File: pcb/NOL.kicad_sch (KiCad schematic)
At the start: 70 parts, among them J1 Conn_01x10_Socket, J10 Conn_01x02_Socket, J11 Conn_01x02_Socket, J12 Conn_01x02_Socket, J13 Conn_01x02_Socket, J14 Conn_01x02_Socket, J15 Conn_01x02_Socket, J16 Conn_01x02_Socket, J17 Conn_01x02_Socket, J18 Conn_01x02_Socket, J19 Conn_01x02_Socket, J2 Conn_01x02_Pin, J20 Conn_01x02_Socket, J21 Conn_01x02_Socket, J22 Conn_01x02_Socket, J23 Conn_01x02_Socket, J24 Conn_01x02_Socket, J25 Conn_01x02_Socket, J26 Conn_01x02_Socket, J27 Conn_01x02_Socket, J28 Conn_01x02_Socket, J29 Conn_01x02_Socket, J3 Conn_01x10_Socket, J30 Conn_01x02_Socket, J31 Conn_01x02_Socket, J32 Conn_01x02_Socket, J33 Conn_01x02_Socket, J4 Conn_02x02_Counter_Clockwise, J5 Conn_02x02_Counter_Clockwise, J6 Conn_02x02_Counter_Clockwise, J7 Conn_02x02_Counter_Clockwise, J8 Conn_02x02_Counter_Clockwise, J9 Conn_02x02_Counter_Clockwise, U1 4001, U2 4001

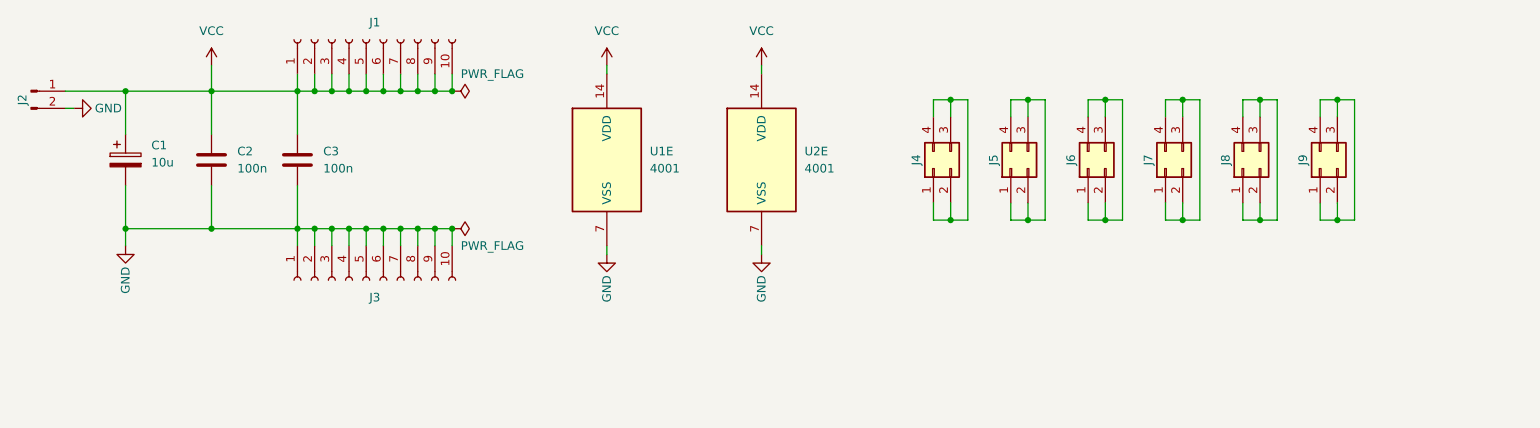
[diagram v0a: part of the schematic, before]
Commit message: Add reverse polarity protection
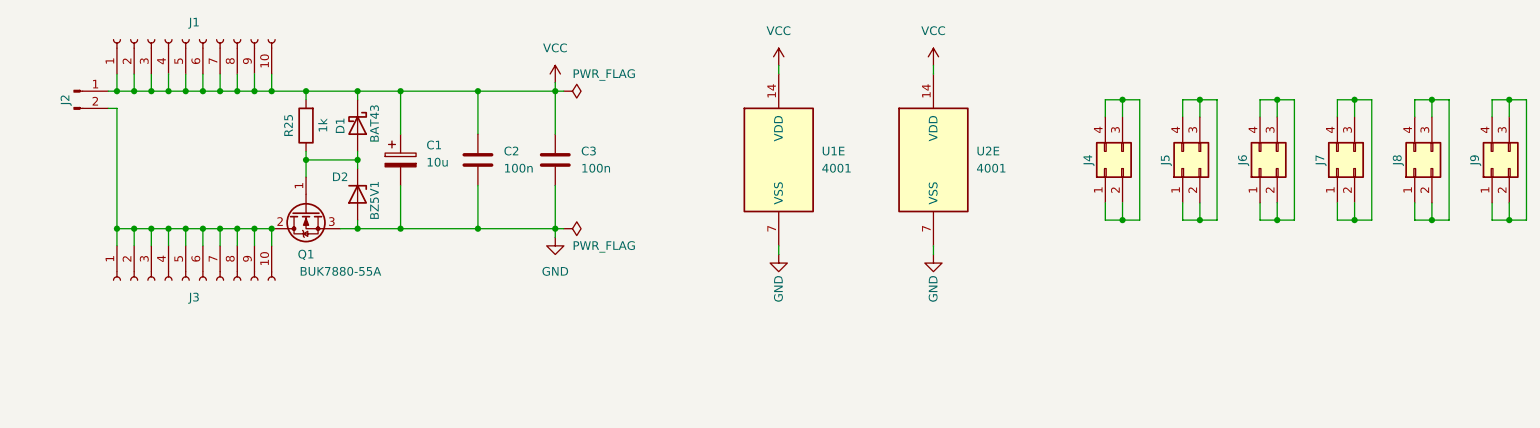
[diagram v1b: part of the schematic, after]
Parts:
- added D1: BAT43, Diode_SMD:D_MiniMELF, symbol Device:D_Schottky
- added D2: BZ5V1, Diode_SMD:D_MiniMELF, symbol Diode:BZV55B15
- added Q1: BUK7880-55A, Package_TO_SOT_SMD:SOT-223-3_TabPin2, symbol Transistor_FET:BUK7880-55A
- added R25: 1k, Resistor_SMD:R_1206_3216Metric, symbol Device:R
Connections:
- net GND: now also D2.2 (A), Q1.3 (S); no longer J2.2 (Pin_2), J3.1 (Pin_1), J3.10 (Pin_10), J3.2 (Pin_2), J3.3 (Pin_3), J3.4 (Pin_4), J3.5 (Pin_5), J3.6 (Pin_6), J3.7 (Pin_7), J3.8 (Pin_8), J3.9 (Pin_9)
- net VCC: now also D1.1 (K), R25.2
- new net: D1.2 (A), D2.1 (K), Q1.1 (G), R25.1
- new net: J2.2 (Pin_2), J3.1 (Pin_1), J3.10 (Pin_10), J3.2 (Pin_2), J3.3 (Pin_3), J3.4 (Pin_4), J3.5 (Pin_5), J3.6 (Pin_6), J3.7 (Pin_7), J3.8 (Pin_8), J3.9 (Pin_9), Q1.2 (D)
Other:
- moved on the sheet: C1, C2, C3, J1, J2, J3, J4, J5, J6, J7, J8, J9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
